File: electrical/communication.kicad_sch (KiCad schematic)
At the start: 13 parts

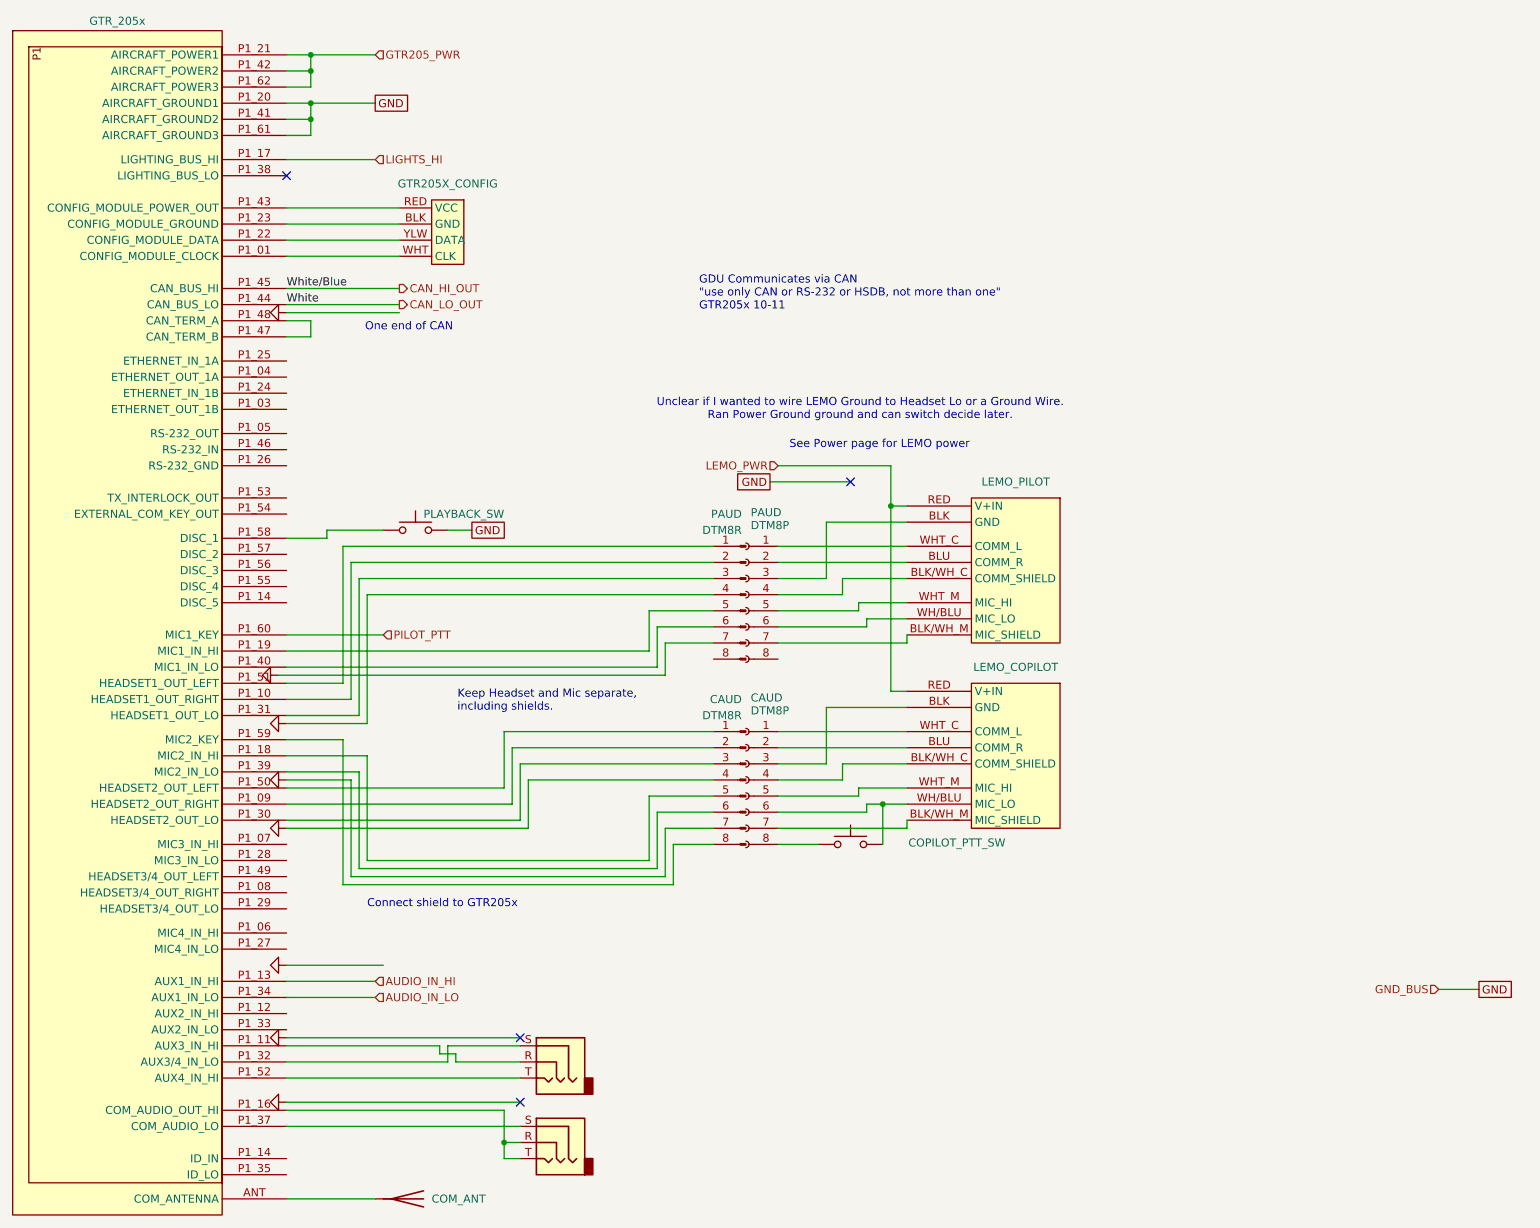
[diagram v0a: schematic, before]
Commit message: Added audio jacks
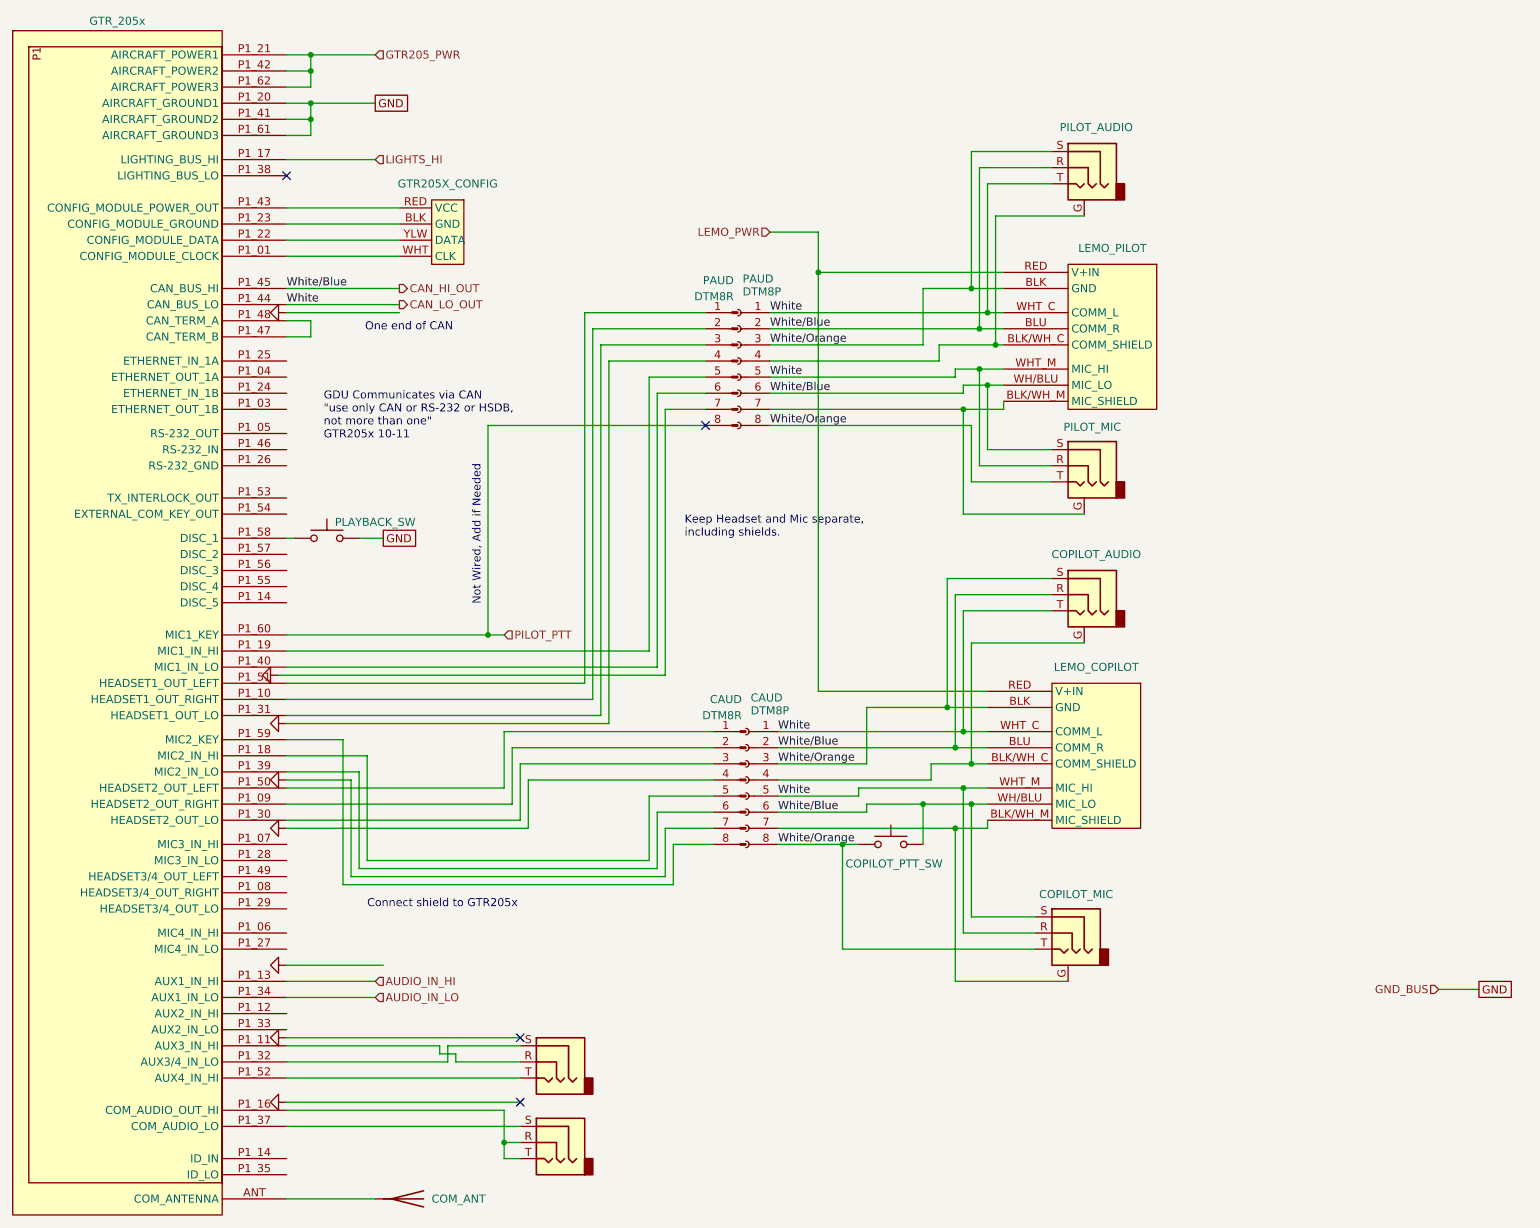
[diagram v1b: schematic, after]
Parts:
- added COPILOT_AUDIO, COPILOT_MIC, PILOT_AUDIO, PILOT_MIC: AudioJack3_Ground, symbol Connector_Audio:AudioJack3_Ground
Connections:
- net CAN_HI_OUT: now also CAUD.2 (Pin_2), CAUD.6 (Pin_6), COPILOT_PTT_SW.2, LEMO_COPILOT.BLU (COMM_R), LEMO_COPILOT.WH/BLU (MIC_LO), LEMO_PILOT.BLU (COMM_R), LEMO_PILOT.WH/BLU (MIC_LO), PAUD.2 (Pin_2), PAUD.6 (Pin_6), COPILOT_AUDIO.R, COPILOT_MIC.S, PILOT_AUDIO.R, PILOT_MIC.S
- net CAN_LO_OUT: now also CAUD.1 (Pin_1), CAUD.5 (Pin_5), LEMO_COPILOT.WHT_C (COMM_L), LEMO_COPILOT.WHT_M (MIC_HI), LEMO_PILOT.WHT_C (COMM_L), LEMO_PILOT.WHT_M (MIC_HI), PAUD.1 (Pin_1), PAUD.5 (Pin_5), COPILOT_AUDIO.T, COPILOT_MIC.R, PILOT_AUDIO.T, PILOT_MIC.R
- net PILOT_PTT: now also PAUD.8 (Pin_8)
- net White/Orange: now reaches LEMO_PILOT.BLK (GND), PAUD.3 (Pin_3)
- net White/Orange: now also CAUD.3 (Pin_3), CAUD.8 (Pin_8), COPILOT_PTT_SW.1, LEMO_COPILOT.BLK (GND), PAUD.8 (Pin_8), COPILOT_AUDIO.S, COPILOT_MIC.T, PILOT_AUDIO.S, PILOT_MIC.T
- net at LEMO_PILOT.BLK/WH_C (COMM_SHIELD), PAUD.4 (Pin_4): now also PILOT_AUDIO.G
- net at LEMO_PILOT.BLK/WH_M (MIC_SHIELD), PAUD.7 (Pin_7): now also PILOT_MIC.G
- net at CAUD.4 (Pin_4), LEMO_COPILOT.BLK/WH_C (COMM_SHIELD): now also COPILOT_AUDIO.G
- net at CAUD.7 (Pin_7), LEMO_COPILOT.BLK/WH_M (MIC_SHIELD): now also COPILOT_MIC.G
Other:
- note added: "Not Wired, Add if Needed"
- note removed: "See Power page for LEMO power"
- note removed: "Unclear if I wanted to wire LEMO Ground to Headset Lo or a Ground Wire. Ran Power Ground ground and can switch decide later."
- moved on the sheet: COPILOT_PTT_SW, LEMO_COPILOT, LEMO_PILOT, PAUD, PLAYBACK_SW

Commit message: Confirmed LEMO to match installation manual, and retained ring terminals.
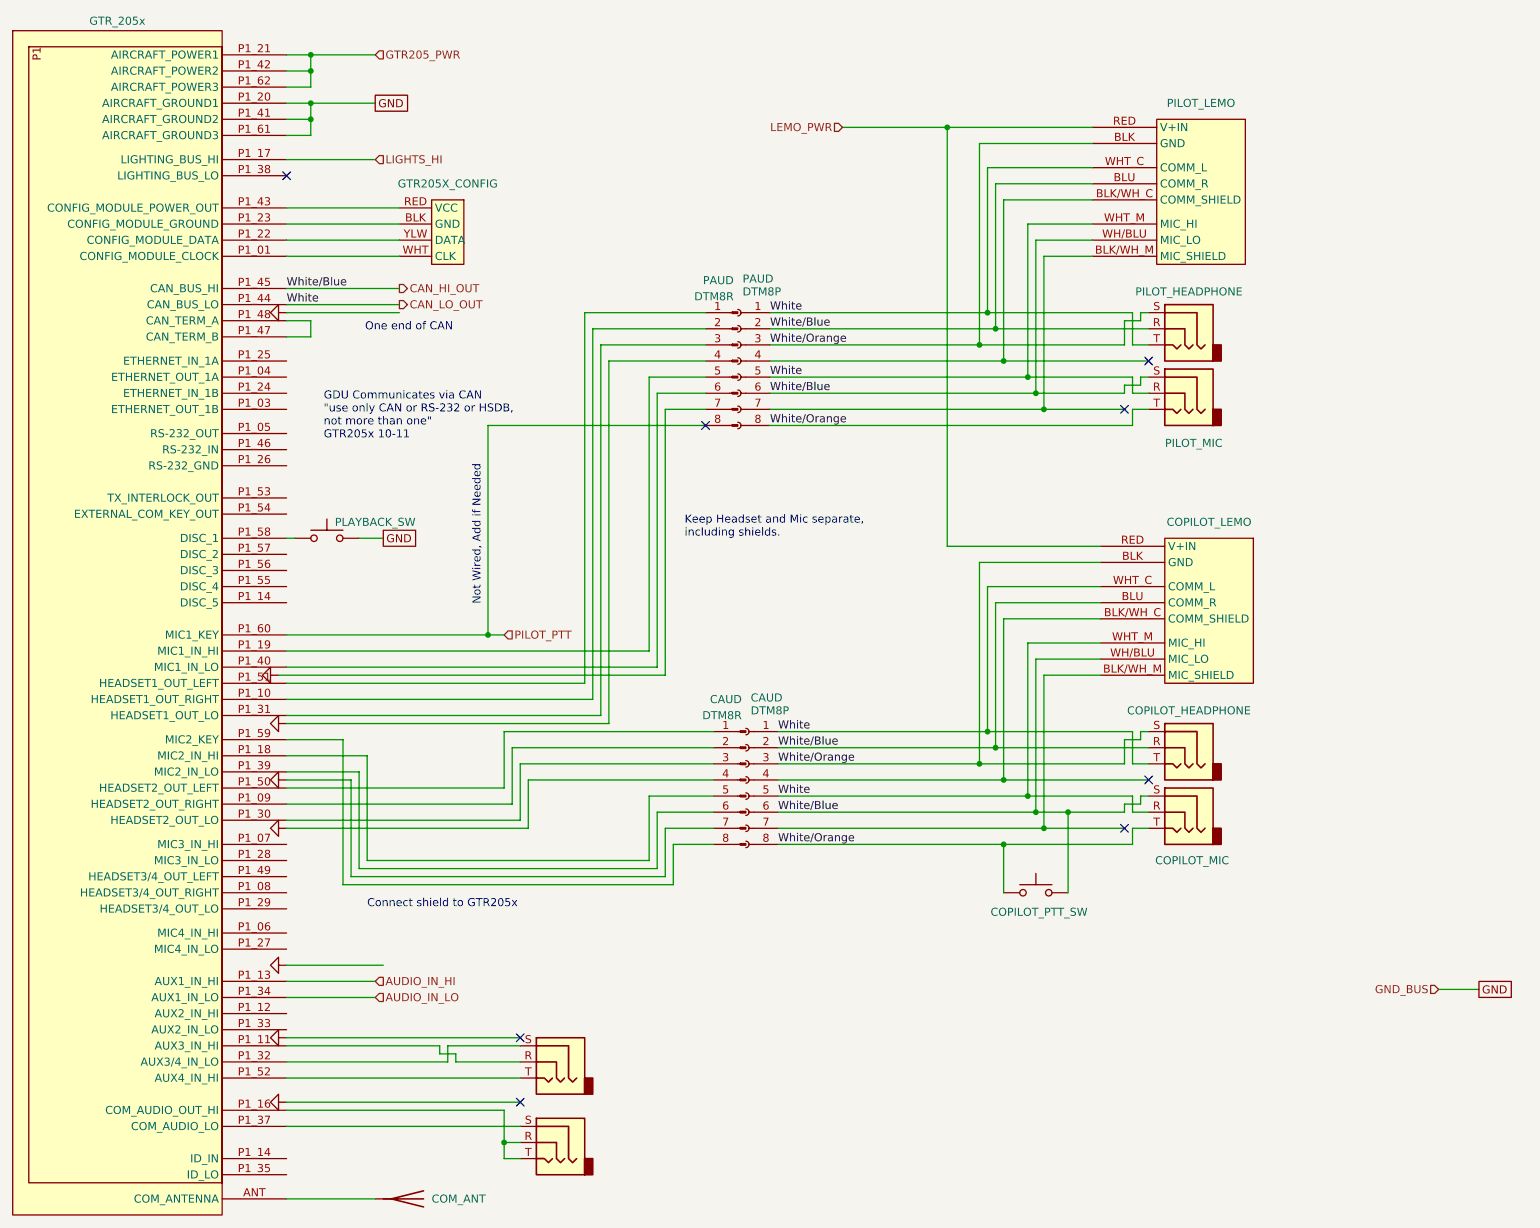
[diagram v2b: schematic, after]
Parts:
- removed COPILOT_AUDIO, COPILOT_MIC, PILOT_AUDIO, PILOT_MIC: AudioJack3_Ground, symbol Connector_Audio:AudioJack3_Ground
- added COPILOT_HEADPHONE, COPILOT_MIC, PILOT_HEADPHONE, PILOT_MIC: AudioJack3, symbol Connector_Audio:AudioJack3
- renumbered LEMO_COPILOT to COPILOT_LEMO, LEMO_PILOT to PILOT_LEMO
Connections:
- net CAN_HI_OUT: now also COPILOT_HEADPHONE.R, COPILOT_MIC.S, PILOT_HEADPHONE.R, PILOT_MIC.S
- net CAN_LO_OUT: now also COPILOT_HEADPHONE.T, COPILOT_MIC.R, PILOT_HEADPHONE.T, PILOT_MIC.R
- net White/Orange: now also COPILOT_HEADPHONE.S, COPILOT_MIC.T, PILOT_HEADPHONE.S, PILOT_MIC.T
- no-connect marks 4 -> 8
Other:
- moved on the sheet: COPILOT_LEMO, COPILOT_PTT_SW, PILOT_LEMO

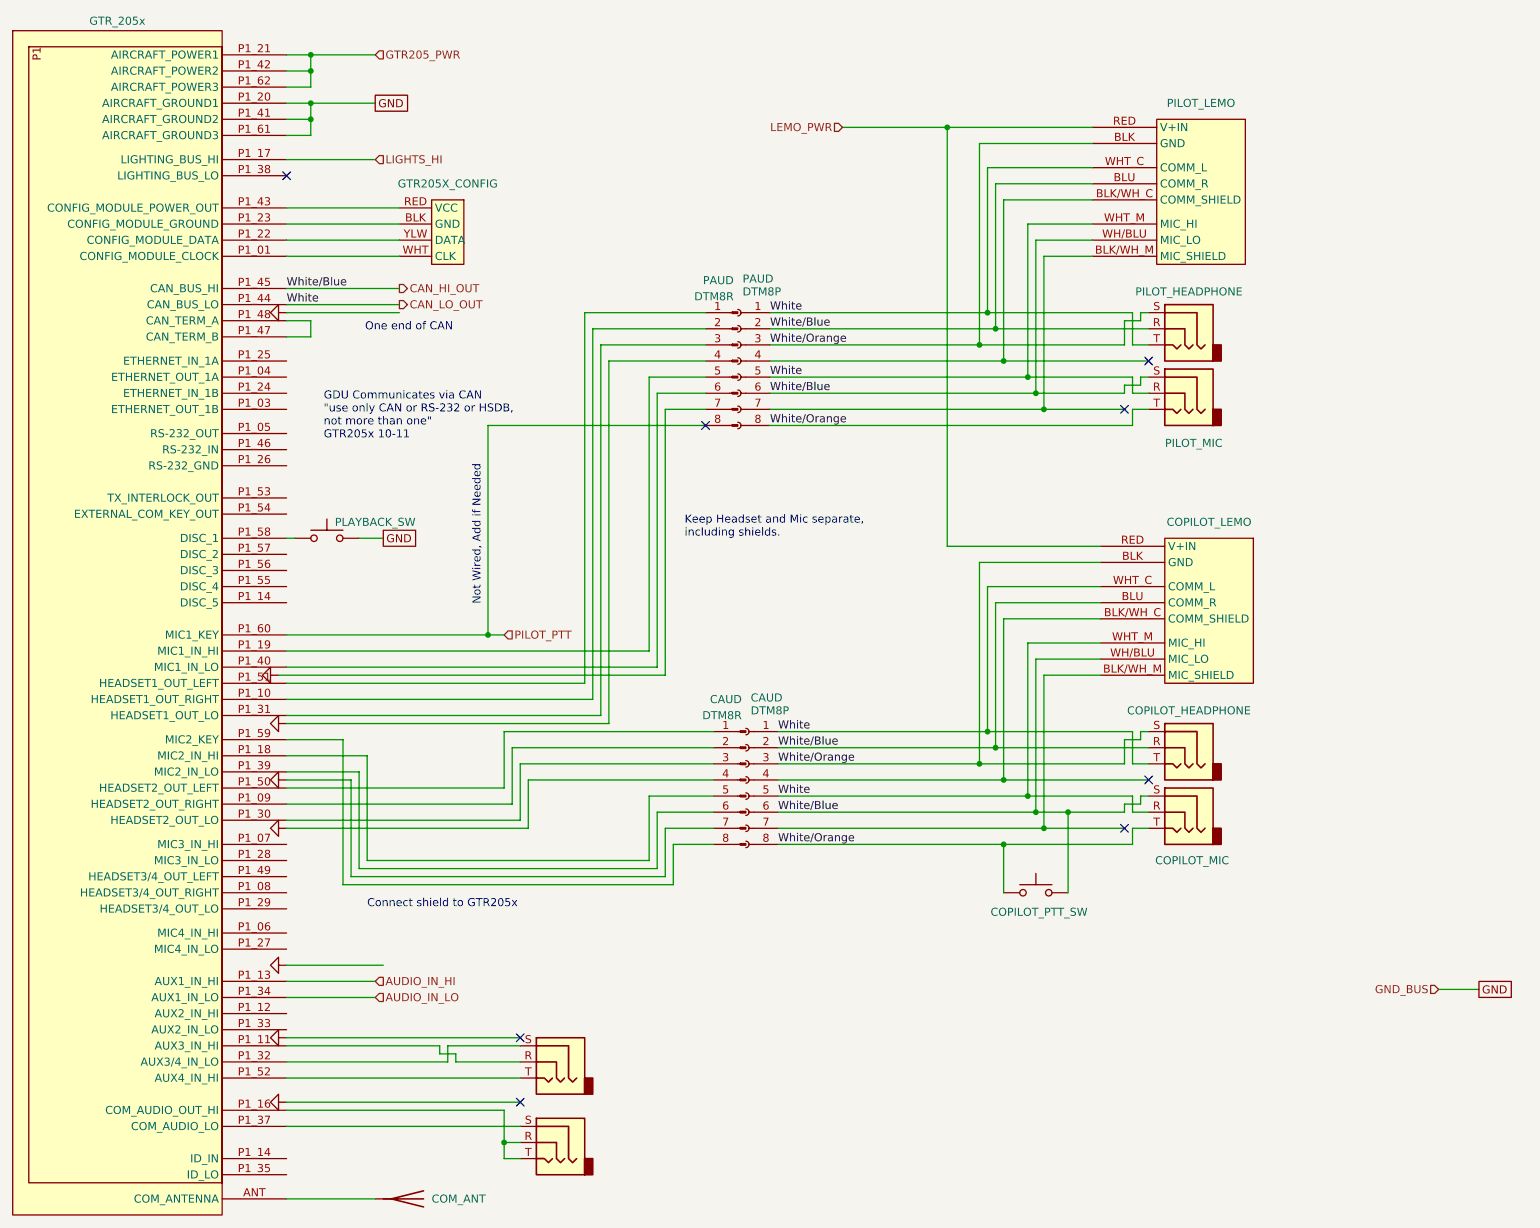
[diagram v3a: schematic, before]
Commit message: Removed non-LEMO connector for comms to just simplify things I won't use.
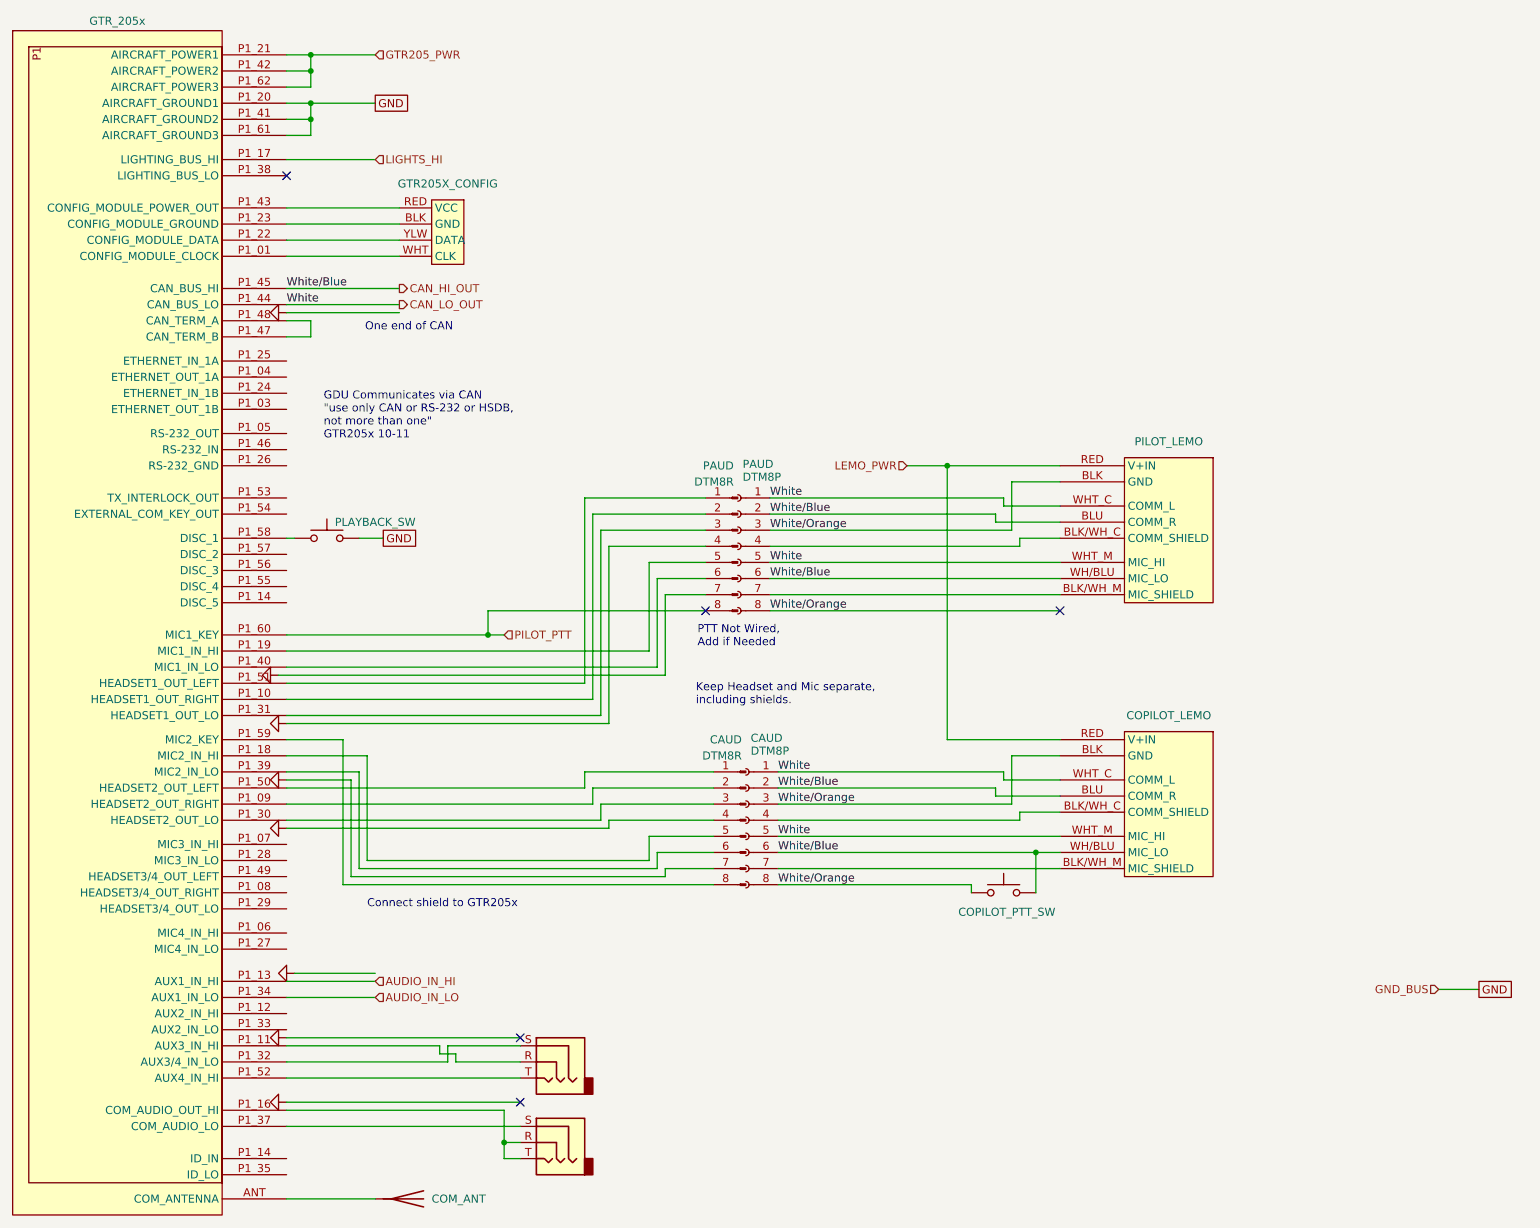
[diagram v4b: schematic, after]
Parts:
- removed COPILOT_HEADPHONE, COPILOT_MIC, PILOT_HEADPHONE, PILOT_MIC: AudioJack3, symbol Connector_Audio:AudioJack3
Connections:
- no-connect marks 8 -> 5
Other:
- note added: "PTT Not Wired, Add if Needed"
- note removed: "Not Wired, Add if Needed"
- moved on the sheet: CAUD, COPILOT_LEMO, COPILOT_PTT_SW, PAUD, PILOT_LEMO
